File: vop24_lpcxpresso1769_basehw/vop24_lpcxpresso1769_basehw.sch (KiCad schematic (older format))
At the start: 17 parts

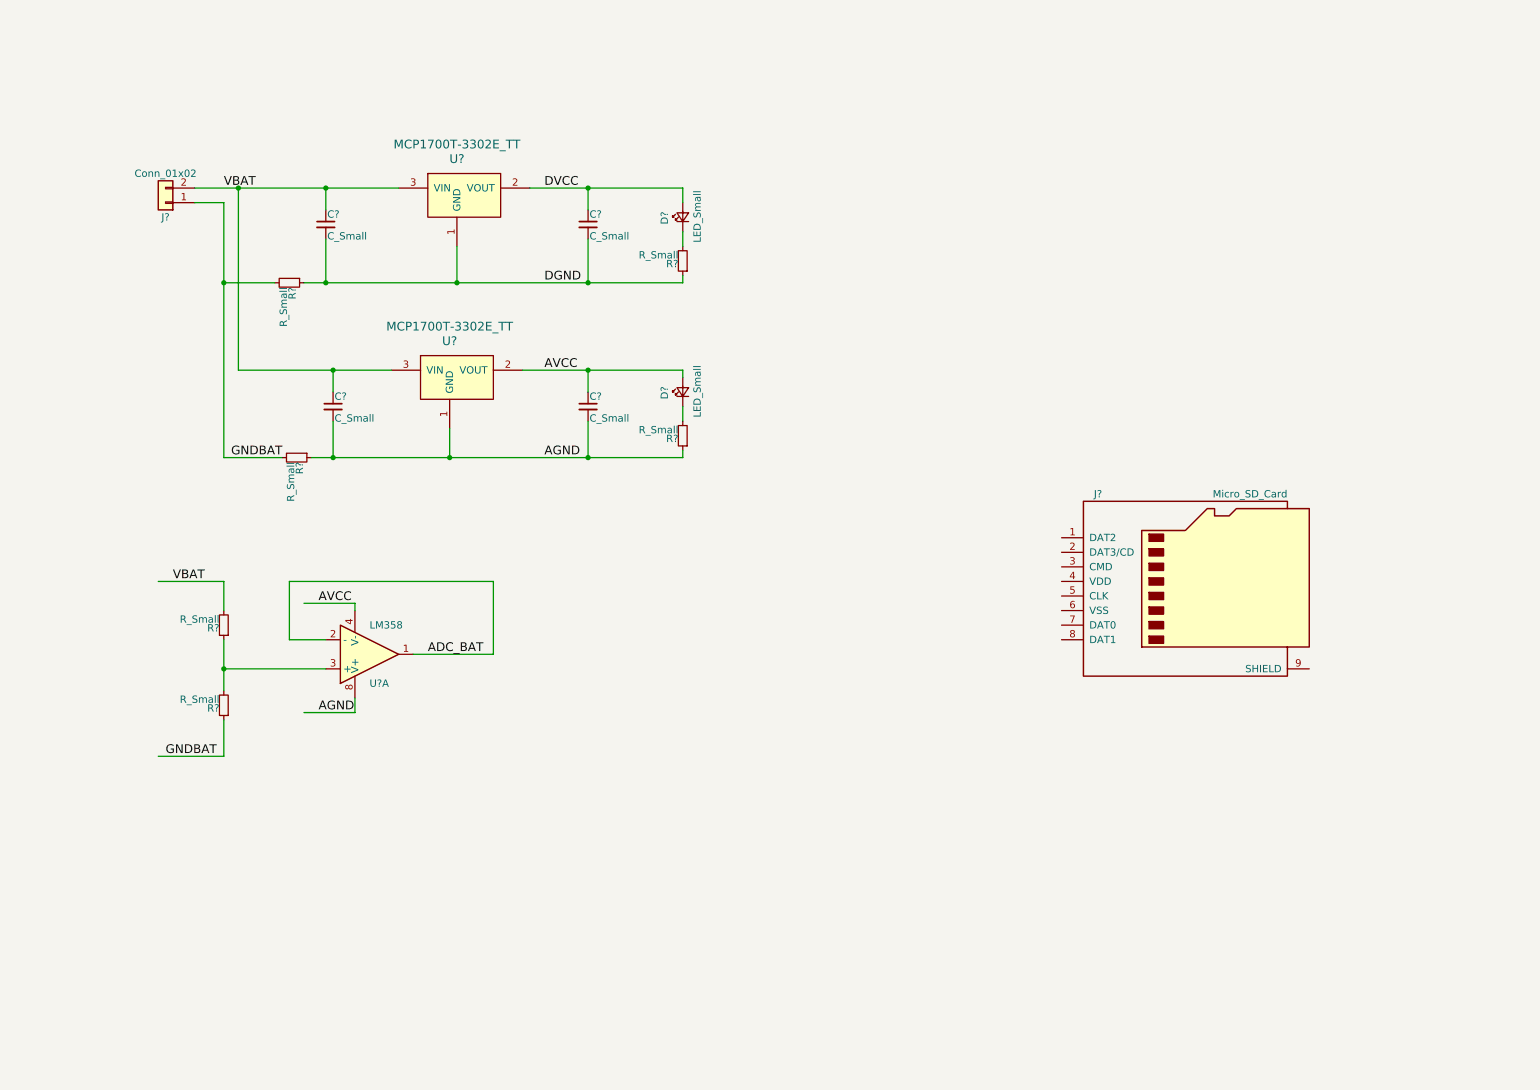
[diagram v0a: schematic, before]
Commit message: Esquematico:    - se agrego simbolo lpcxpresso1769
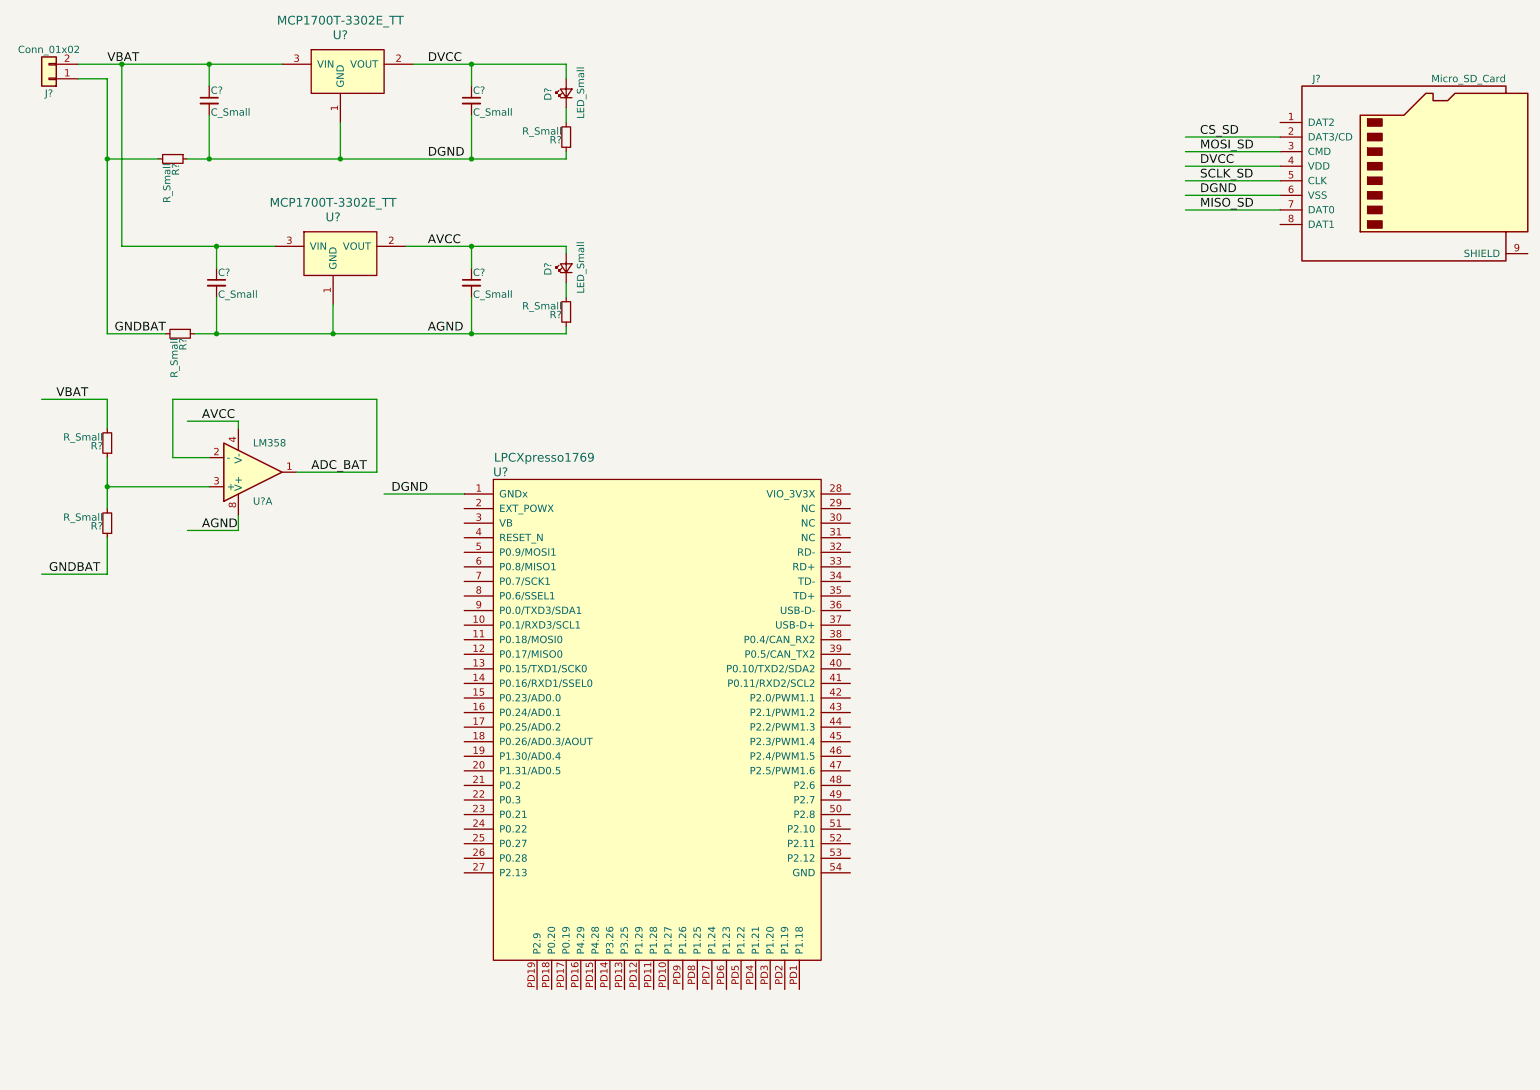
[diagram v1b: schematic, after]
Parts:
- added U?: LPCXpresso1769, symbol LPCXpresso1769
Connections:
- net labels added: CS_SD, MISO_SD, MOSI_SD, SCLK_SD
- wire segments 42 -> 49
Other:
- moved on the sheet: C?, D?, J?, R?, U?, U?A

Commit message: Esquematico:    - conexion SD con lpc1769
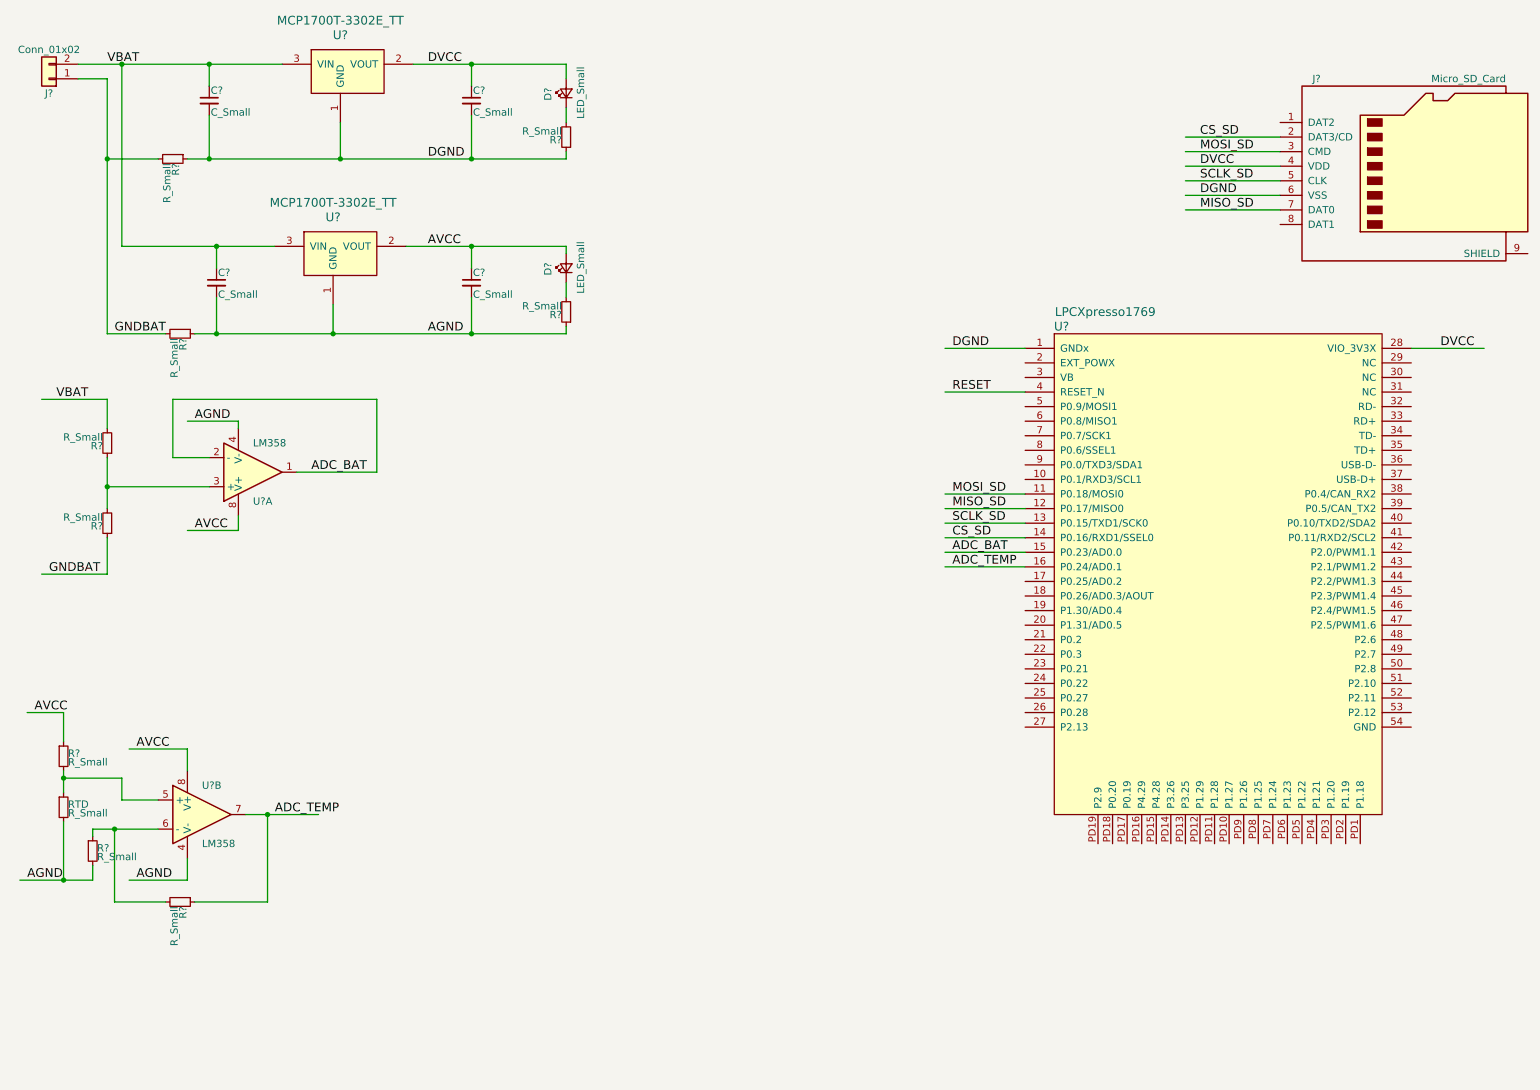
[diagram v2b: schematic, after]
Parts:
- added R? (x3), RTD: R_Small, symbol R_Small
- added U?: LM358, symbol LM358
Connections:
- net labels added: ADC_TEMP, RESET
- wire segments 49 -> 78
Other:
- moved on the sheet: U?
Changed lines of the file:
@@
 LIBS:dk_Alarms-Buzzers-and-Sirens
 LIBS:dk_Addressable-Specialty
-LIBS:lpcxpresso1769
 LIBS:vop24_lpcxpresso1769_basehw-cache
 EELAYER 25 0
@@
 Text Label 800  4350 0    60   ~ 0
 GNDBAT
-Text Label 1850 3300 0    60   ~ 0
+Text Label 1800 4050 0    60   ~ 0
 AVCC
-Text Label 1850 4050 0    60   ~ 0
+Text Label 1400 6450 0    60   ~ 0
 AGND
 Text Label 2600 3650 0    60   ~ 0
@@
 	-1   0    0    1
 $EndComp
-Wire Wire Line
-	1000 850  2400 850
-Wire Wire Line
-	1900 1000 1900 850
-Connection ~ 1900 850
-Wire Wire Line
-	1300 2100 2350 2100
-Wire Wire Line
-	1300 2100 1300 850
-Connection ~ 1300 850
-Wire Wire Line
-	1950 2250 1950 2100
-Connection ~ 1950 2100
-Wire Wire Line
-	3250 2100 4350 2100
-Wire Wire Line
-	3700 2100 3700 2250
-Wire Wire Line
-	1950 2450 1950 2700
-Wire Wire Line
-	1800 2700 4350 2700
-Wire Wire Line
-	3700 2700 3700 2450
-Wire Wire Line
-	2750 2500 2750 2700
-Connection ~ 2750 2700
-Wire Wire Line
-	1900 1200 1900 1500
-Wire Wire Line
-	1750 1500 4350 1500
-Wire Wire Line
-	3700 1500 3700 1200
-Wire Wire Line
-	3300 850  4350 850
-Wire Wire Line
-	3700 850  3700 1000
-Wire Wire Line
-	2800 1250 2800 1500
-Connection ~ 2800 1500
-Connection ~ 1950 2700
-Wire Wire Line
-	1200 2700 1600 2700
-Wire Wire Line
-	1200 950  1200 2700
-Wire Wire Line
-	1200 950  1000 950
-Wire Wire Line
-	1550 1500 1200 1500
-Connection ~ 1200 1500
-Connection ~ 1900 1500
-Wire Wire Line
-	1200 3350 1200 3150
-Wire Wire Line
-	1200 3150 750  3150
-Wire Wire Line
-	1200 3550 1200 3900
-Wire Wire Line
-	1200 4100 1200 4350
-Wire Wire Line
-	1200 4350 750  4350
-Wire Wire Line
-	1900 3750 1200 3750
-Connection ~ 1200 3750
-Wire Wire Line
-	1900 3550 1650 3550
-Wire Wire Line
-	1650 3550 1650 3150
-Wire Wire Line
-	1650 3150 3050 3150
-Wire Wire Line
-	3050 3150 3050 3650
-Wire Wire Line
-	3050 3650 2500 3650
-Wire Wire Line
-	2100 3350 2100 3300
-Wire Wire Line
-	2100 3300 1750 3300
-Wire Wire Line
-	2100 3950 2100 4050
-Wire Wire Line
-	2100 4050 1750 4050
-Wire Wire Line
-	4350 850  4350 950
-Connection ~ 3700 850
-Wire Wire Line
-	4350 1250 4350 1150
-Wire Wire Line
-	4350 1500 4350 1450
-Connection ~ 3700 1500
-Wire Wire Line
-	4350 2100 4350 2150
-Connection ~ 3700 2100
-Wire Wire Line
-	4350 2350 4350 2450
-Wire Wire Line
-	4350 2700 4350 2650
-Connection ~ 3700 2700
-Wire Wire Line
-	9250 1350 8600 1350
-Wire Wire Line
-	9250 1450 8600 1450
-Wire Wire Line
-	9250 1550 8600 1550
-Wire Wire Line
-	9250 1650 8600 1650
-Wire Wire Line
-	9250 1750 8600 1750
-Wire Wire Line
-	9250 1850 8600 1850
 Text Label 8700 1350 0    60   ~ 0
 CS_SD
@@
 L LPCXpresso1769 U?
 U 1 1 5B343F3C
-P 5000 5350
-F 0 "U?" H 3900 7050 60  0000 C CNN
-F 1 "LPCXpresso1769" H 4200 7150 60  0000 C CNN
-F 2 "" H 4700 5750 60  0001 C CNN
-F 3 "" H 4700 5750 60  0001 C CNN
-	1    5000 5350
-	1    0    0    -1
-$EndComp
-Wire Wire Line
-	3650 3800 3100 3800
-Text Label 3150 3800 0    60   ~ 0
+P 8850 4350
+F 0 "U?" H 7750 6050 60  0000 C CNN
+F 1 "LPCXpresso1769" H 8050 6150 60  0000 C CNN
+F 2 "" H 8550 4750 60  0001 C CNN
+F 3 "" H 8550 4750 60  0001 C CNN
+	1    8850 4350
+	1    0    0    -1
+$EndComp
+Text Label 7000 2800 0    60   ~ 0
 DGND
+Text Label 7000 4200 0    60   ~ 0
+ADC_BAT
+Text Label 7000 4300 0    60   ~ 0
+ADC_TEMP
+Text Label 10350 2800 0    60   ~ 0
+DVCC
+Text Label 7000 3100 0    60   ~ 0
+RESET
+$Comp
+L LM358 U?
+U 2 1 5B36A538
+P 1850 6000
+F 0 "U?" H 1850 6200 50  0000 L CNN
+F 1 "LM358" H 1850 5800 50  0000 L CNN
+F 2 "" H 1850 6000 50  0001 C CNN
+F 3 "" H 1850 6000 50  0001 C CNN
+	2    1850 6000
+	1    0    0    -1
+$EndComp
+$Comp
+L R_Small R?
+U 1 1 5B36A603
+P 900 5600
+F 0 "R?" H 930 5620 50  0000 L CNN
+F 1 "R_Small" H 930 5560 50  0000 L CNN
+F 2 "" H 900 5600 50  0001 C CNN
+F 3 "" H 900 5600 50  0001 C CNN
+	1    900  5600
+	1    0    0    -1
+$EndComp
+$Comp
+L R_Small RTD
+U 1 1 5B36A698
+P 900 5950
+F 0 "RTD" H 930 5970 50  0000 L CNN
+F 1 "R_Small" H 930 5910 50  0000 L CNN
+F 2 "" H 900 5950 50  0001 C CNN
+F 3 "" H 900 5950 50  0001 C CNN
+	1    900  5950
+	1    0    0    -1
+$EndComp
+$Comp
+L R_Small R?
+U 1 1 5B36A6F3
+P 1100 6250
+F 0 "R?" H 1130 6270 50  0000 L CNN
+F 1 "R_Small" H 1130 6210 50  0000 L CNN
+F 2 "" H 1100 6250 50  0001 C CNN
+F 3 "" H 1100 6250 50  0001 C CNN
+	1    1100 6250
+	1    0    0    -1
+$EndComp
+$Comp
+L R_Small R?
+U 1 1 5B36A779
+P 1700 6600
+F 0 "R?" H 1730 6620 50  0000 L CNN
+F 1 "R_Small" H 1730 6560 50  0000 L CNN
+F 2 "" H 1700 6600 50  0001 C CNN
+F 3 "" H 1700 6600 50  0001 C CNN
+	1    1700 6600
+	0    1    1    0
+$EndComp
+Text Label 1400 5550 0    60   ~ 0
+AVCC
+Text Label 700  5300 0    60   ~ 0
+AVCC
+Wire Wire Line
+	1000 850  2400 850
+Wire Wire Line
+	1900 1000 1900 850
+Connection ~ 1900 850
+Wire Wire Line
+	1300 2100 2350 2100
+Wire Wire Line
+	1300 2100 1300 850
+Connection ~ 1300 850
+Wire Wire Line
+	1950 2250 1950 2100
+Connection ~ 1950 2100
+Wire Wire Line
+	3250 2100 4350 2100
+Wire Wire Line
+	3700 2100 3700 2250
+Wire Wire Line
+	1950 2450 1950 2700
+Wire Wire Line
+	1800 2700 4350 2700
+Wire Wire Line
+	3700 2700 3700 2450
+Wire Wire Line
+	2750 2500 2750 2700
+Connection ~ 2750 2700
+Wire Wire Line
+	1900 1200 1900 1500
+Wire Wire Line
+	1750 1500 4350 1500
+Wire Wire Line
+	3700 1500 3700 1200
+Wire Wire Line
+	3300 850  4350 850
+Wire Wire Line
+	3700 850  3700 1000
+Wire Wire Line
+	2800 1250 2800 1500
+Connection ~ 2800 1500
+Connection ~ 1950 2700
+Wire Wire Line
+	1200 2700 1600 2700
+Wire Wire Line
+	1200 950  1200 2700
+Wire Wire Line
+	1200 950  1000 950
+Wire Wire Line
+	1550 1500 1200 1500
+Connection ~ 1200 1500
+Connection ~ 1900 1500
+Wire Wire Line
+	1200 3350 1200 3150
+Wire Wire Line
+	1200 3150 750  3150
+Wire Wire Line
+	1200 3550 1200 3900
+Wire Wire Line
+	1200 4100 1200 4350
+Wire Wire Line
+	1200 4350 750  4350
+Wire Wire Line
+	1900 3750 1200 3750
+Connection ~ 1200 3750
+Wire Wire Line
+	1900 3550 1650 3550
+Wire Wire Line
+	1650 3550 1650 3150
+Wire Wire Line
+	1650 3150 3050 3150
+Wire Wire Line
+	3050 3150 3050 3650
+Wire Wire Line
+	3050 3650 2500 3650
+Wire Wire Line
+	2100 3350 2100 3300
+Wire Wire Line
+	2100 3300 1750 3300
+Wire Wire Line
+	2100 3950 2100 4050
+Wire Wire Line
+	2100 4050 1750 4050
+Wire Wire Line
+	4350 850  4350 950
+Connection ~ 3700 850
+Wire Wire Line
+	4350 1250 4350 1150
+Wire Wire Line
+	4350 1500 4350 1450
+Connection ~ 3700 1500
+Wire Wire Line
+	4350 2100 4350 2150
+Connection ~ 3700 2100
+Wire Wire Line
+	4350 2350 4350 2450
+Wire Wire Line
+	4350 2700 4350 2650
+Connection ~ 3700 2700
+Wire Wire Line
+	9250 1350 8600 1350
+Wire Wire Line
+	9250 1450 8600 1450
+Wire Wire Line
+	9250 1550 8600 1550
+Wire Wire Line
+	9250 1650 8600 1650
+Wire Wire Line
+	9250 1750 8600 1750
+Wire Wire Line
+	9250 1850 8600 1850
+Wire Wire Line
+	7500 2800 6950 2800
+Wire Wire Line
+	7500 4200 6950 4200
+Wire Wire Line
+	7500 4300 6950 4300
+Wire Wire Line
+	10150 2800 10650 2800
+Wire Wire Line
+	7500 3100 6950 3100
+Wire Wire Line
+	1750 5700 1750 5550
+Wire Wire Line
+	1750 5550 1350 5550
+Wire Wire Line
+	1750 6300 1750 6450
+Wire Wire Line
+	1750 6450 1350 6450
+Wire Wire Line
+	900  5500 900  5300
+Wire Wire Line
+	900  5300 650  5300
+Wire Wire Line
+	900  5700 900  5850
+Wire Wire Line
+	900  6050 900  6450
+Wire Wire Line
+	1100 6450 1100 6350
+Text Label 650  6450 0    60   ~ 0
+AGND
+Wire Wire Line
+	1100 6150 1100 6150
+Wire Wire Line
+	1100 6150 1100 6100
+Wire Wire Line
+	1100 6100 1550 6100
+Wire Wire Line
+	1550 5900 1300 5900
+Wire Wire Line
+	1300 5900 1300 5750
+Wire Wire Line
+	1300 5750 900  5750
+Connection ~ 900  5750
+Wire Wire Line
+	1250 6100 1250 6600
+Wire Wire Line
+	1250 6600 1600 6600
+Connection ~ 1250 6100
+Wire Wire Line
+	2150 6000 2650 6000
+Wire Wire Line
+	1800 6600 2300 6600
+Wire Wire Line
+	2300 6600 2300 6000
+Connection ~ 2300 6000
+Text Label 2350 6000 0    60   ~ 0
+ADC_TEMP
+Wire Wire Line
+	600  6450 1100 6450
+Connection ~ 900  6450
+Text Label 1800 3300 0    60   ~ 0
+AGND
+Wire Wire Line
+	7500 3800 6950 3800
+Wire Wire Line
+	6950 3900 7500 3900
+Wire Wire Line
+	7500 4000 6950 4000
+Wire Wire Line
+	7500 4100 6950 4100
+Text Label 7000 3800 0    60   ~ 0
+MOSI_SD
+Text Label 7000 3900 0    60   ~ 0
+MISO_SD
+Text Label 7000 4000 0    60   ~ 0
+SCLK_SD
+Text Label 7000 4100 0    60   ~ 0
+CS_SD
 $EndSCHEMATC

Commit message: Esquematico:    - ads1292 con conexiones parcial
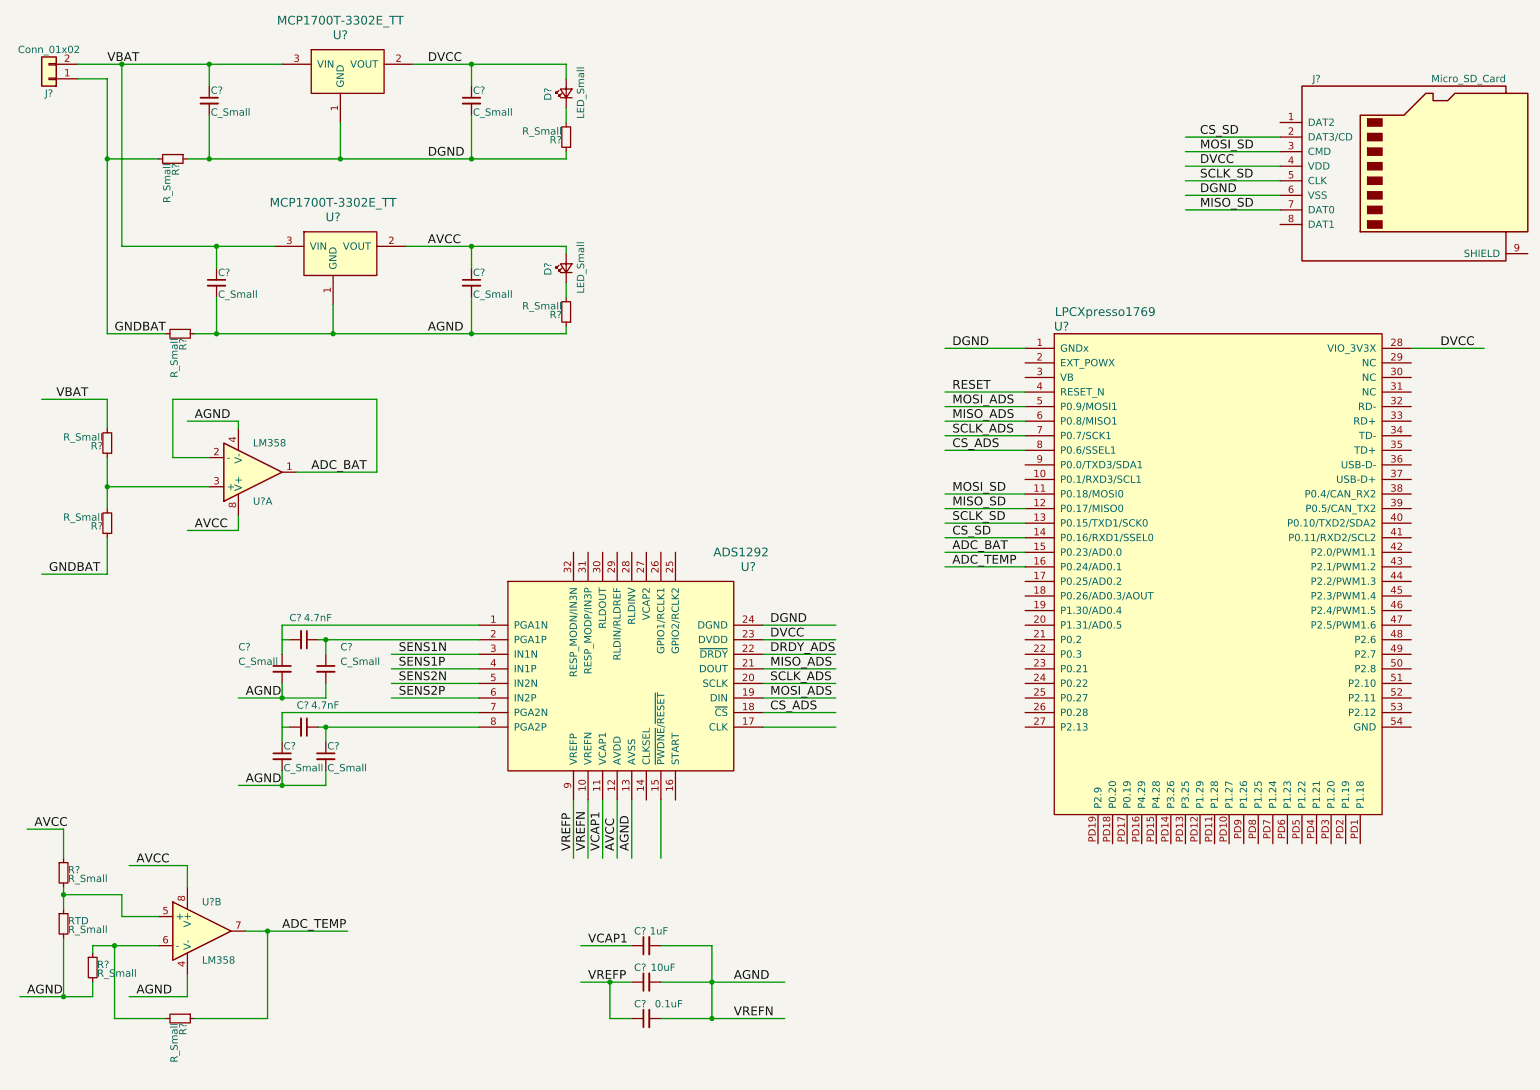
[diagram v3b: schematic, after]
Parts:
- added C? (x4): C_Small, symbol C_Small
- added C? (x2): 4.7nF, symbol C_Small
- added C?: 1uF, symbol C_Small
- added C?: 10uF, symbol C_Small
- added C?: 0.1uF, symbol C_Small
- added U?: ADS1292, symbol ADS1292
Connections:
- net labels added: CS_ADS, DRDY_ADS, MISO_ADS, MOSI_ADS, SCLK_ADS, SENS1N, SENS1P, SENS2N, SENS2P, VCAP1, VREFN, VREFP
- wire segments 78 -> 124
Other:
- moved on the sheet: R?, RTD, U?B
